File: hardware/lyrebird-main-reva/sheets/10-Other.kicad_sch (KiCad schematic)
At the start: 3 parts, among them J4 12 V 2.1 x 5.5 mm, centre pos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

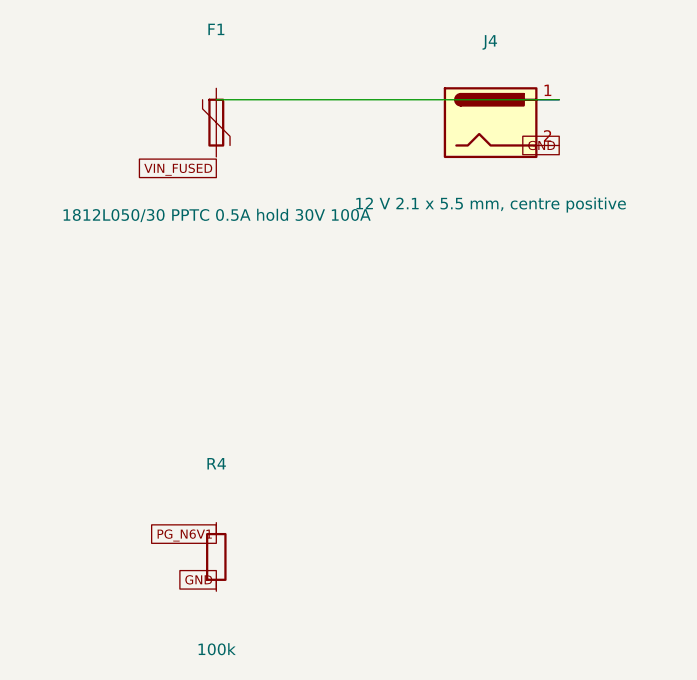
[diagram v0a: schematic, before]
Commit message: Connect two power-good nets that were connected to nothing
The schematic validator found a confirmed fault, and it is the kind that
reads as correct code. `Net("PG_5V")` appears twice in main_board.py --
once to attach the buck's power-good pin, once to attach its pull-up --
and SKiDL creates a NEW net on each call, uniquifying the second name.
The result was four single-node nets: both LMR33630 power-good pins
alone, and both 100 k resistors with one lead floating.

The inverter's half mattered more than the buck's. U7's GND pin *is*
-6V_A, so 100 k to system ground is a pull-up relative to the device and
the only way that flag can be read at all. It was reading nothing.

Both now use one Net object and reuse it, which is what every other net
in both generators already did -- the defect was exactly two instances of
one idiom, not a pattern. I checked: MCLK is also written as
Net("MCLK") twice, but once per file on different boards, so it is
whole in each netlist.

The more useful outcome is a check. A net with one node connects
nothing, and nothing in the generation path said so -- KiCad ERC would
have, on import, and nothing runs ERC. check_freshness.py now reports
single-node nets on both boards, with the module's four reserved element
lines exempted because interface.md requires the main board to drive
them and they are correctly bare on the module side. Tamper-tested by
reintroducing the idiom: it names PG_5V and PG_5V1 and fails.

Co-Authored-By: Claude Opus 5 <noreply@anthropic.com>
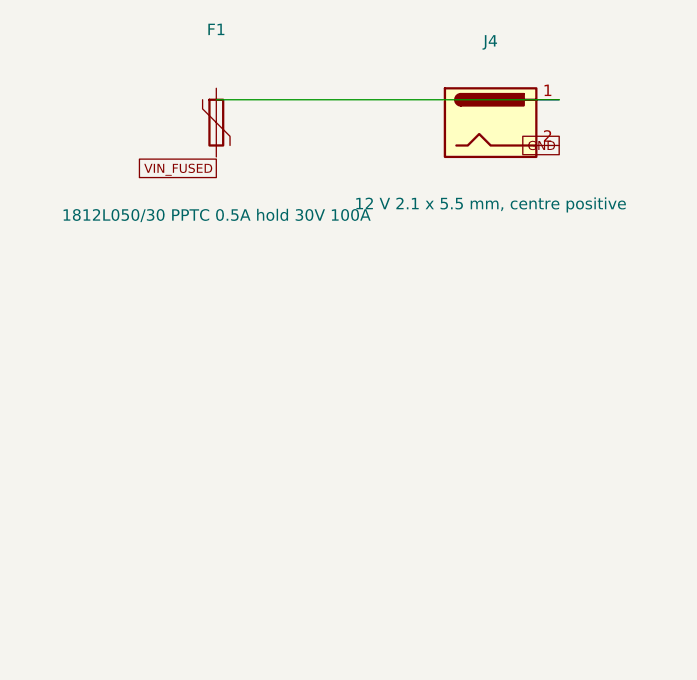
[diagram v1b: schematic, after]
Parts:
- removed R4: 100k, symbol Device:R
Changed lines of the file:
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@@
 	(version 20231120)
 	(generator "lyrebird")
-	(paper "User" 114 121)
+	(paper "User" 114 74)
 	(title_block (title "Other"))
 	(symbol (lib_id "Device:Polyfuse") (at 35.56 35.56 0) (unit 1)
@@
 		(instances (project "" (path "/" (reference "J4") (unit 1))))
 	)
-	(symbol (lib_id "Device:R") (at 35.56 83.82000000000001 0) (unit 1)
-		(exclude_from_sim no) (in_bom yes) (on_board yes) (dnp no)
-		(property "Reference" "R4" (at 35.56 73.51 0)
-			(effects (font (size 1.27 1.27))))
-		(property "Value" "100k" (at 35.56 94.13000000000001 0)
-			(effects (font (size 1.27 1.27))))
-		(instances (project "" (path "/" (reference "R4") (unit 1))))
-	)
 	(wire (pts (xy 35.56 33.02) (xy 73.66 33.02))
 		(stroke (width 0) (type default)))
@@
 		(effects (font (size 1.0 1.0)) (justify right))
 )
-	(global_label "GND" (shape passive) (at 35.56 86.36 0)
-		(effects (font (size 1.0 1.0)) (justify right))
-)
-	(global_label "PG_N6V1" (shape passive) (at 35.56 81.28 0)
-		(effects (font (size 1.0 1.0)) (justify right))
-)
